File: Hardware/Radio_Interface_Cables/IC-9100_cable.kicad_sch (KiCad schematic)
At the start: 4 parts, among them J26 DIN-13, J5 RJ45, J7 6.25 mm Plug, J8 3.5 mm Plug

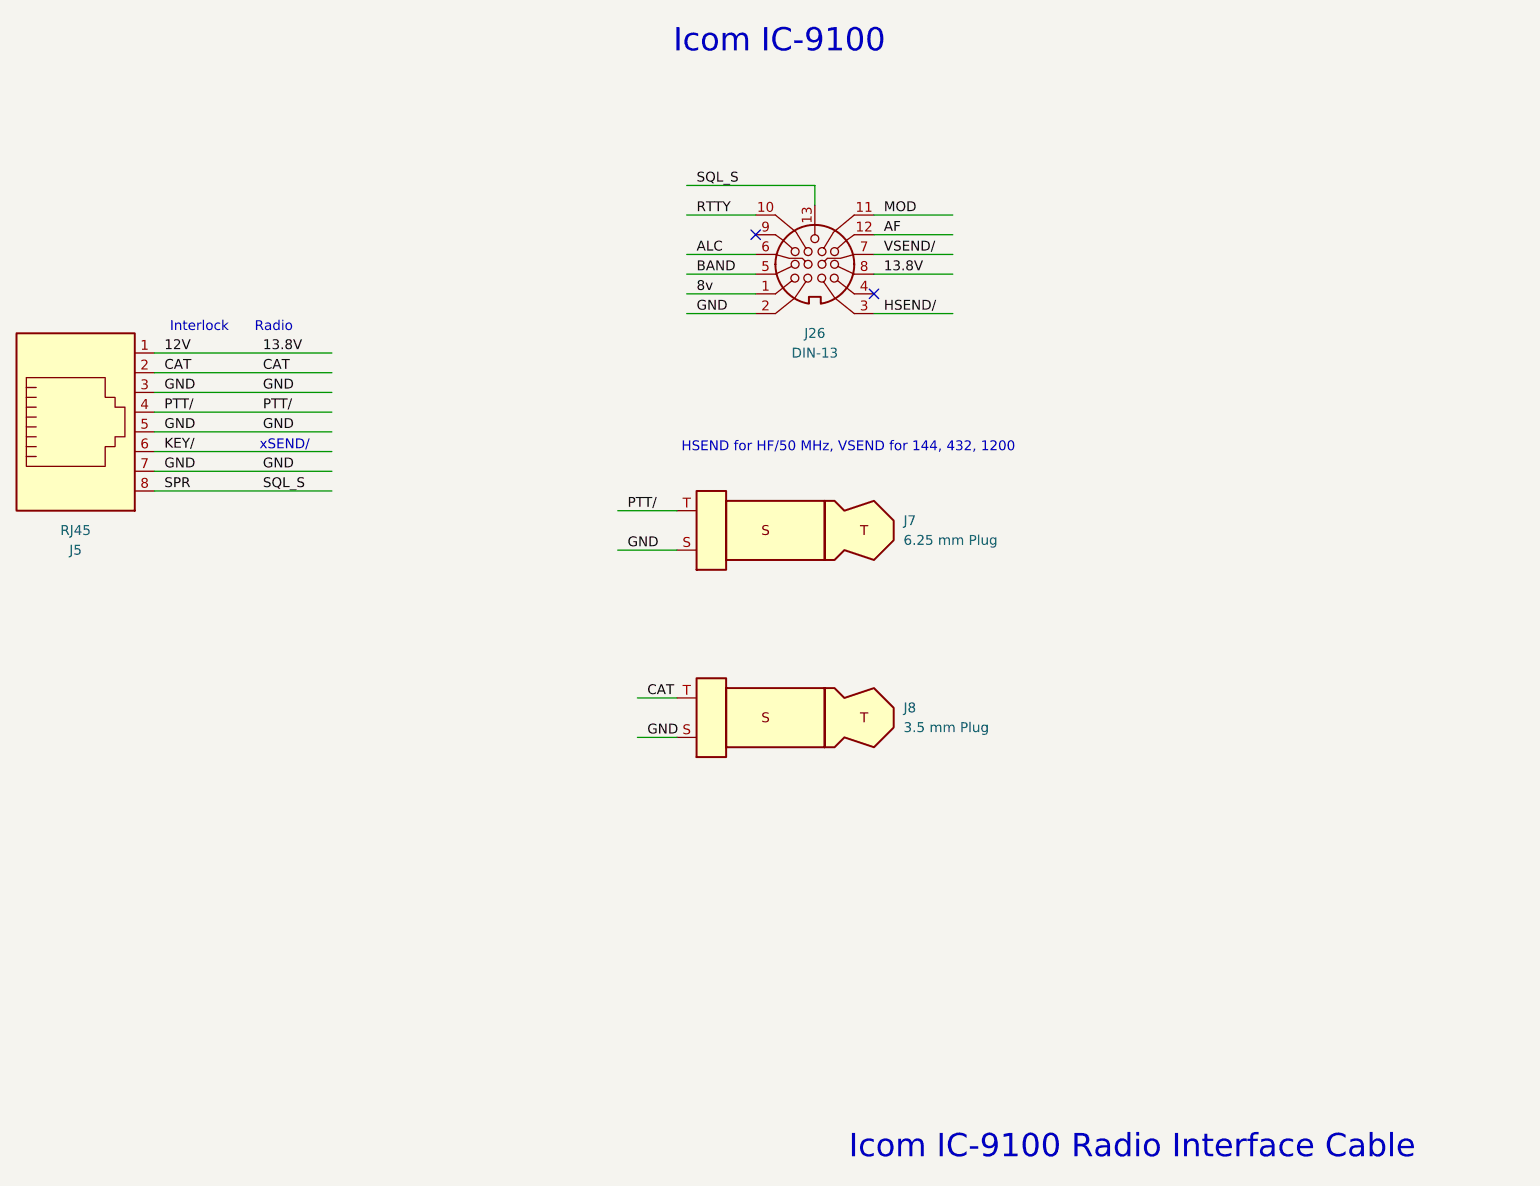
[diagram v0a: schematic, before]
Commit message: Add PTT and CAT connectors on Radio Interface Cables Mark pins as unused
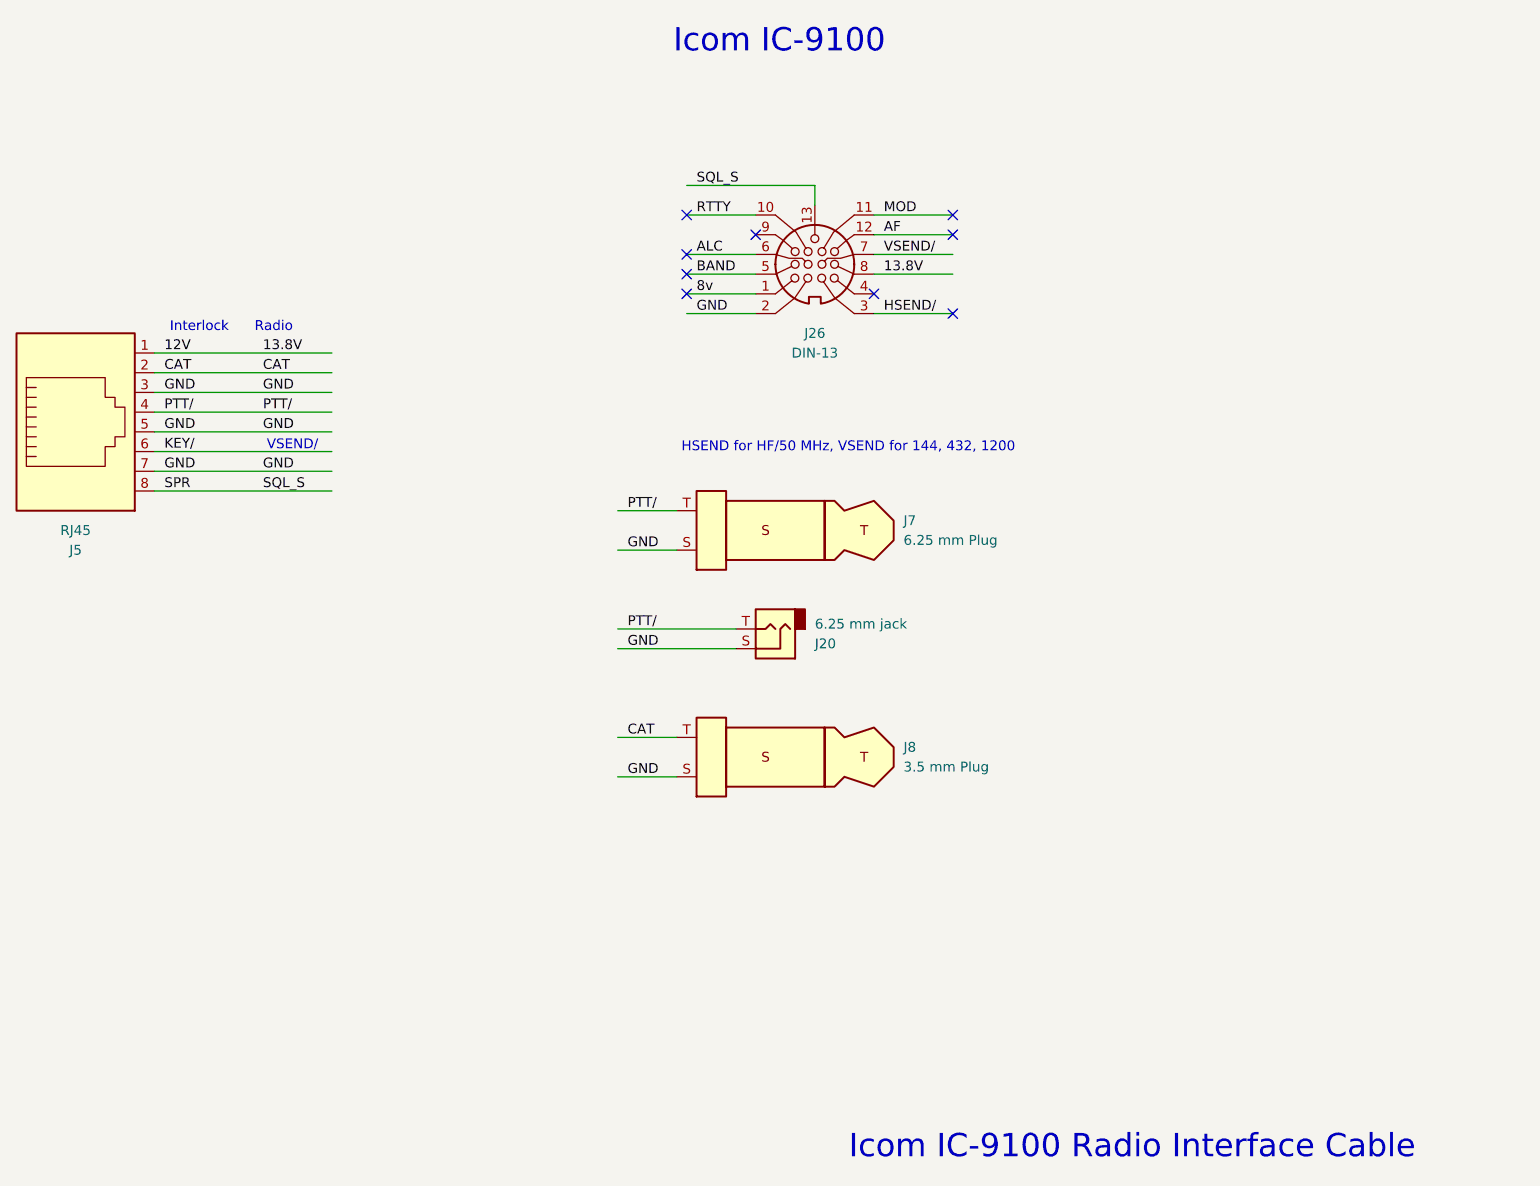
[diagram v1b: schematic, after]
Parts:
- added J20: 6.25 mm jack, symbol Connector_Audio:AudioJack2
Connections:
- net GND: now also J20.S
- net PTT/: now also J20.T
- no-connect marks 2 -> 9
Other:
- note added: "VSEND/"
- note removed: "xSEND/"
- moved on the sheet: J8
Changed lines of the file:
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@@
 		)
 	)
-	(text "xSEND/"
+	(text "VSEND/"
 		(exclude_from_sim no)
-		(at 112.014 83.058 0)
-		(effects
-			(font
-				(size 1.27 1.27)
-			)
-		)
+		(at 113.03 83.058 0)
+		(effects
+			(font
+				(size 1.27 1.27)
+			)
+		)
+	)
+	(no_connect
+		(at 163.83 58.42)
 	)
 	(no_connect
@@
 	)
 	(no_connect
+		(at 163.83 60.96)
+	)
+	(no_connect
+		(at 198.12 55.88)
+	)
+	(no_connect
+		(at 163.83 53.34)
+	)
+	(no_connect
+		(at 198.12 53.34)
+	)
+	(no_connect
+		(at 198.12 66.04)
+	)
+	(no_connect
 		(at 187.96 63.5)
 	)
+	(no_connect
+		(at 163.83 63.5)
+	)
+	(wire
+		(pts
+			(xy 154.94 106.68) (xy 170.18 106.68)
+		)
+		(stroke
+			(width 0)
+			(type default)
+		)
+	)
 	(wire
 		(pts
@@
 	(wire
 		(pts
-			(xy 157.48 115.57) (xy 162.56 115.57)
+			(xy 154.94 120.65) (xy 162.56 120.65)
+		)
+		(stroke
+			(width 0)
+			(type default)
+		)
+	)
+	(wire
+		(pts
+			(xy 154.94 109.22) (xy 170.18 109.22)
 		)
 		(stroke
@@
 	(wire
 		(pts
-			(xy 157.48 120.65) (xy 162.56 120.65)
+			(xy 154.94 125.73) (xy 162.56 125.73)
 		)
 		(stroke
@@
 	)
 	(label "CAT"
-		(at 158.75 115.57 0)
+		(at 156.21 120.65 0)
 		(effects
 			(font
@@
 		)
 	)
+	(label "GND"
+		(at 156.21 109.22 0)
+		(effects
+			(font
+				(size 1.27 1.27)
+			)
+			(justify left bottom)
+		)
+	)
 	(label "PTT{slash}"
 		(at 96.52 78.74 0)
@@
 		)
 	)
+	(label "PTT{slash}"
+		(at 156.21 106.68 0)
+		(effects
+			(font
+				(size 1.27 1.27)
+			)
+			(justify left bottom)
+		)
+	)
 	(label "GND"
 		(at 109.22 76.2 0)
@@
 	)
 	(label "GND"
-		(at 158.75 120.65 0)
+		(at 156.21 125.73 0)
 		(effects
 			(font
@@
 	(symbol
 		(lib_id "Connector_Audio:AudioPlug2")
-		(at 177.8 118.11 180)
+		(at 177.8 123.19 180)
 		(unit 1)
 		(exclude_from_sim no)
@@
 		(fields_autoplaced yes)
 		(property "Reference" "J8"
-			(at 191.77 116.8399 0)
+			(at 191.77 121.9199 0)
 			(effects
 				(font
@@
 		)
 		(property "Value" "3.5 mm Plug"
-			(at 191.77 119.3799 0)
+			(at 191.77 124.4599 0)
 			(effects
 				(font
@@
 		)
 		(property "Footprint" ""
-			(at 168.91 116.84 0)
+			(at 168.91 121.92 0)
 			(effects
 				(font
@@
 		)
 		(property "Datasheet" "~"
-			(at 168.91 116.84 0)
+			(at 168.91 121.92 0)
 			(effects
 				(font
@@
 		)
 		(property "Description" "Audio Jack, 2 Poles (Mono / TS)"
-			(at 177.8 118.11 0)
+			(at 177.8 123.19 0)
 			(effects
 				(font
@@
 					(unit 1)
 				)
+			)
+		)
+	)
+	(symbol
+		(lib_id "Connector_Audio:AudioJack2")
+		(at 175.26 106.68 180)
+		(unit 1)
+		(exclude_from_sim no)
+		(in_bom yes)
+		(on_board yes)
+		(dnp no)
+		(property "Reference" "J20"
+			(at 180.34 108.5851 0)
+			(effects
+				(font
+					(size 1.27 1.27)
+				)
+				(justify right)
+			)
+		)
+		(property "Value" "6.25 mm jack"
+			(at 180.34 106.0451 0)
+			(effects
+				(font
+					(size 1.27 1.27)
+				)
+				(justify right)
+			)
+		)
+		(property "Footprint" ""
+			(at 175.26 106.68 0)
+			(effects
+				(font
+					(size 1.27 1.27)
+				)
+				(hide yes)
+			)
+		)
+		(property "Datasheet" "~"
+			(at 175.26 106.68 0)
+			(effects
+				(font
+					(size 1.27 1.27)
+				)
+				(hide yes)
+			)
+		)
+		(property "Description" "Audio Jack, 2 Poles (Mono / TS)"
+			(at 175.26 106.68 0)
+			(effects
+				(font
+					(size 1.27 1.27)
+				)
+				(hide yes)
+			)
+		)
+		(pin "S"
+		)
+		(pin "T"
+		)
+		(instances
+			(project "Radio_Interface_Cables"
+				(path "/65a6842f-7ce8-4a1d-bd27-c5cbbec442dc/9a3b6a31-c5ba-44a2-a058-0e79ebe5f829"
+					(reference "J20")
+					(unit 1)
+				)
